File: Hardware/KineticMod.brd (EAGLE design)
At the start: 80 x 32 mm, 32 parts, among them Q1 AOD417, U1 PCA9685

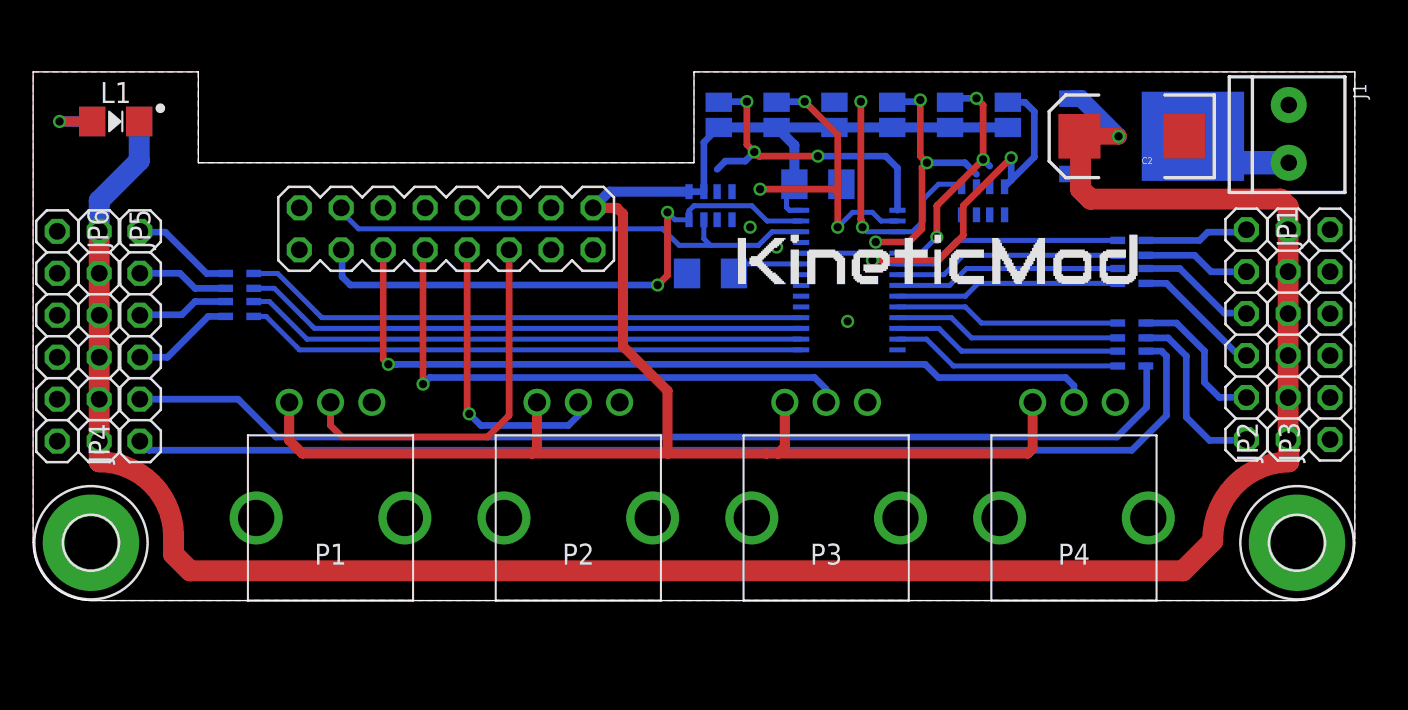
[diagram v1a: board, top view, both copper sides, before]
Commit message: Updated capacitors: - C2 replaced by 470uF 2917 (7343) - Added C3 470uF 2917 (7343)
Updated silkscreen
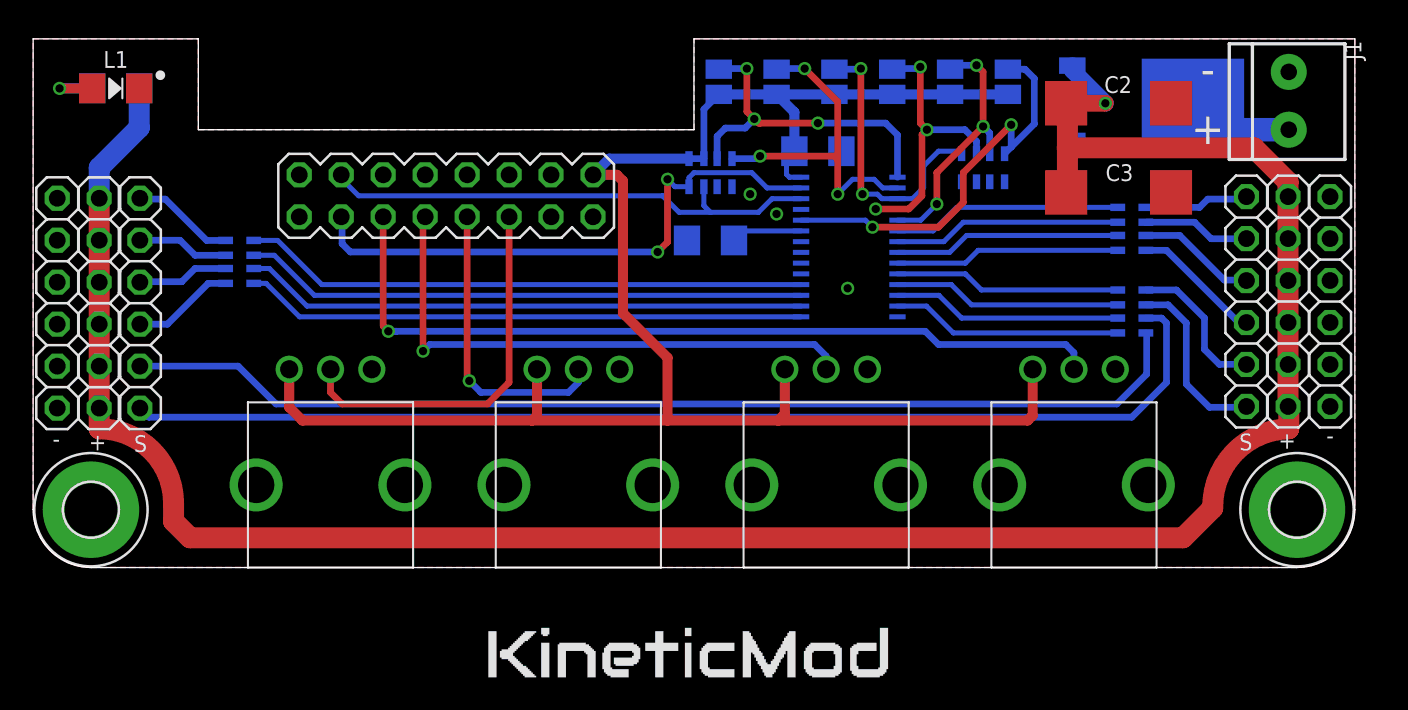
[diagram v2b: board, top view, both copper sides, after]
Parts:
- added C3: 470uF, rcl:D/7343-31R
- C2: value (none) -> 470uF; device SparkFun:EIA7343 -> rcl:D/7343-31R
- moved C2 2.15 mm to (65.7, 28.1)
- moved JP1 2.00 mm to (73.4, 16.1)
- moved JP2 2.00 mm to (76.0, 16.1)
- moved JP3 2.00 mm to (78.5, 16.1)
- moved C1 2.00 mm to (47.5, 25.2)
- moved H1 2.00 mm to (3.50, 3.50)
- moved H2 2.00 mm to (76.5, 3.50)
- moved J1 2.00 mm to (76.0, 28.3)
- moved JP4 2.00 mm to (6.46, 16.0)
- moved JP5 2.00 mm to (4.00, 16.0)
- moved JP6 2.00 mm to (1.46, 16.0)
- moved L1 2.00 mm to (5.00, 29.0)
- moved P1 2.00 mm to (18.0, 5.00)
- moved P2 2.00 mm to (33.0, 5.00)
- moved P3 2.00 mm to (48.0, 5.00)
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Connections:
- net 5.0V: now also C2.+, C3.+; no longer C2.A
- net GND: now also C2.-, C3.-; no longer C2.C
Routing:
- net 5.0V: track 137.6 -> 144.7 mm
- net AD1: track 19.3 -> 20.9 mm
- net AD4: track 14.5 -> 16.1 mm
- net AD0: track 19.7 -> 21.1 mm
- net AD2: track 16.2 -> 17.4 mm
- net AD3: track 17.5 -> 18.3 mm
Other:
- board text added: "+"
- board text added: "-"
- board text added: "S"
